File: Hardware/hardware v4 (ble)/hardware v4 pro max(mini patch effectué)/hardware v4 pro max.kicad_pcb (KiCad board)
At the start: 6 copper layers, 26.4 x 19 mm, 78 parts, among them IC1 MLPF-WB-01E3, IC2 W25Q128JVPIQ_TR, J1 SM06B-SRSS-TB, J3 OLED, J4 USB_C_Receptacle_USB2.0_14P, Q1 2N7002K, SW1 Int, SW4 boot, SW5 RSTBTN, U1 STM32WB55CGUx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

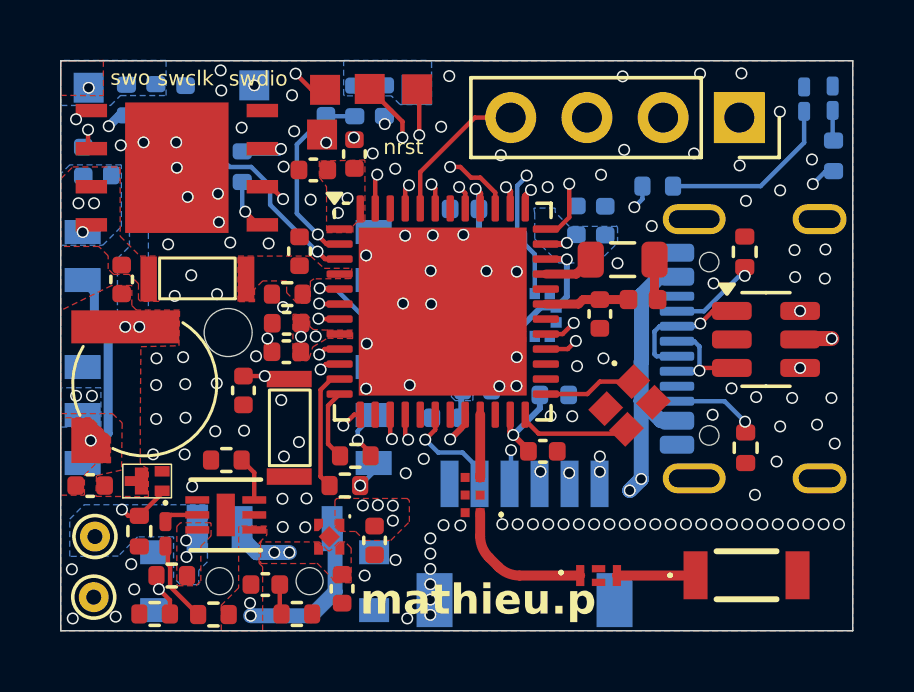
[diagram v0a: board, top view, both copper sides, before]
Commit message: board v5 gps 25Hz !!
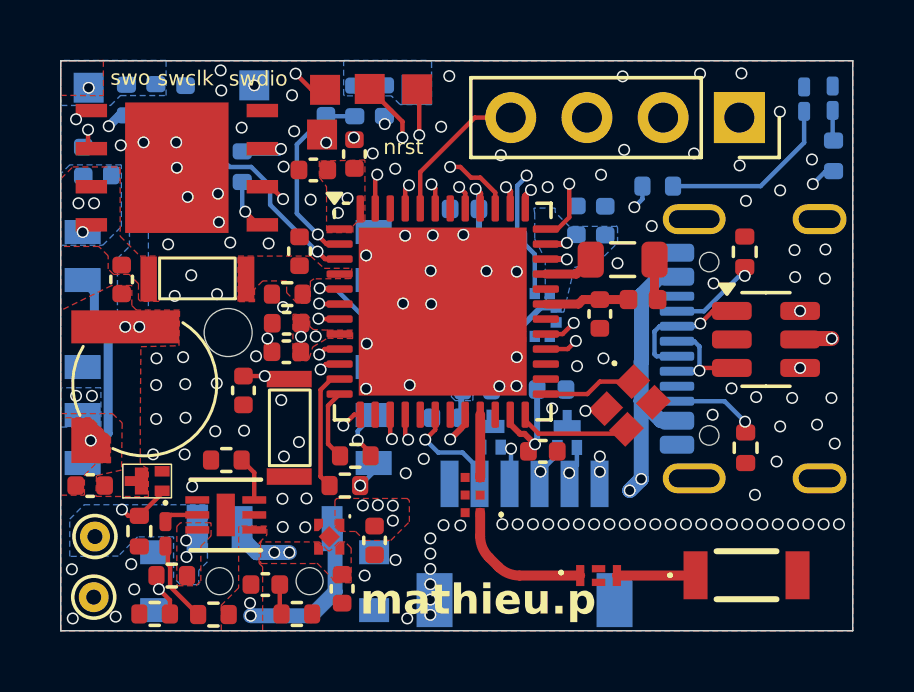
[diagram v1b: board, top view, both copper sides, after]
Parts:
- added D4: MMBZ33VB-QBZ, MMBZ33VB-QBZ:BC847BQBZ, B.Cu at (140.3, 103.4)
- added D5: MMBZ33VB-QBZ, MMBZ33VB-QBZ:BC847BQBZ, B.Cu at (142.8, 103.4)
- moved C13 0.20 mm to (142.3, 102.0)
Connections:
- WSEN-PADS1 pad 5: unconnected-(WSEN-PADS1-SAO-Pad5) -> +3.3V
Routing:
- net +3.3V: track 17.5 -> 16.1 mm
- net USART_TX: track 3.67 -> 4.91 mm
- net COMPASSCL: track 18.4 -> 19.4 mm
- net COMPASSDA: track 26.3 -> 27.2 mm
